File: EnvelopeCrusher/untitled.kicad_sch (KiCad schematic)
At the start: 7 parts

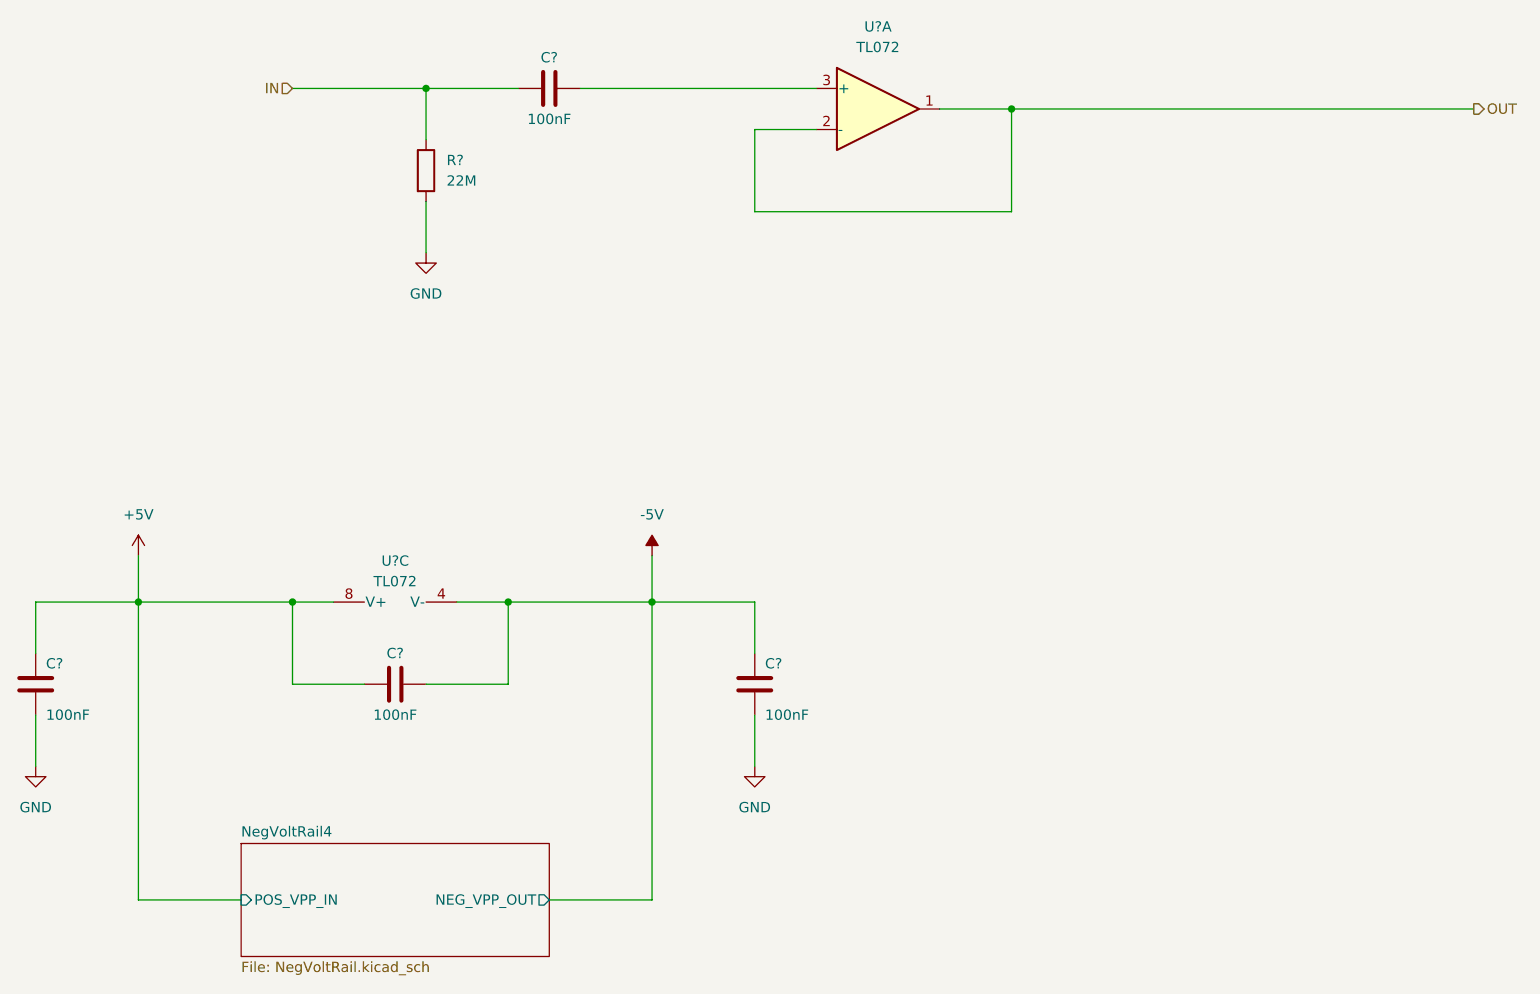
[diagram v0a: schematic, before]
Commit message: updated signal path
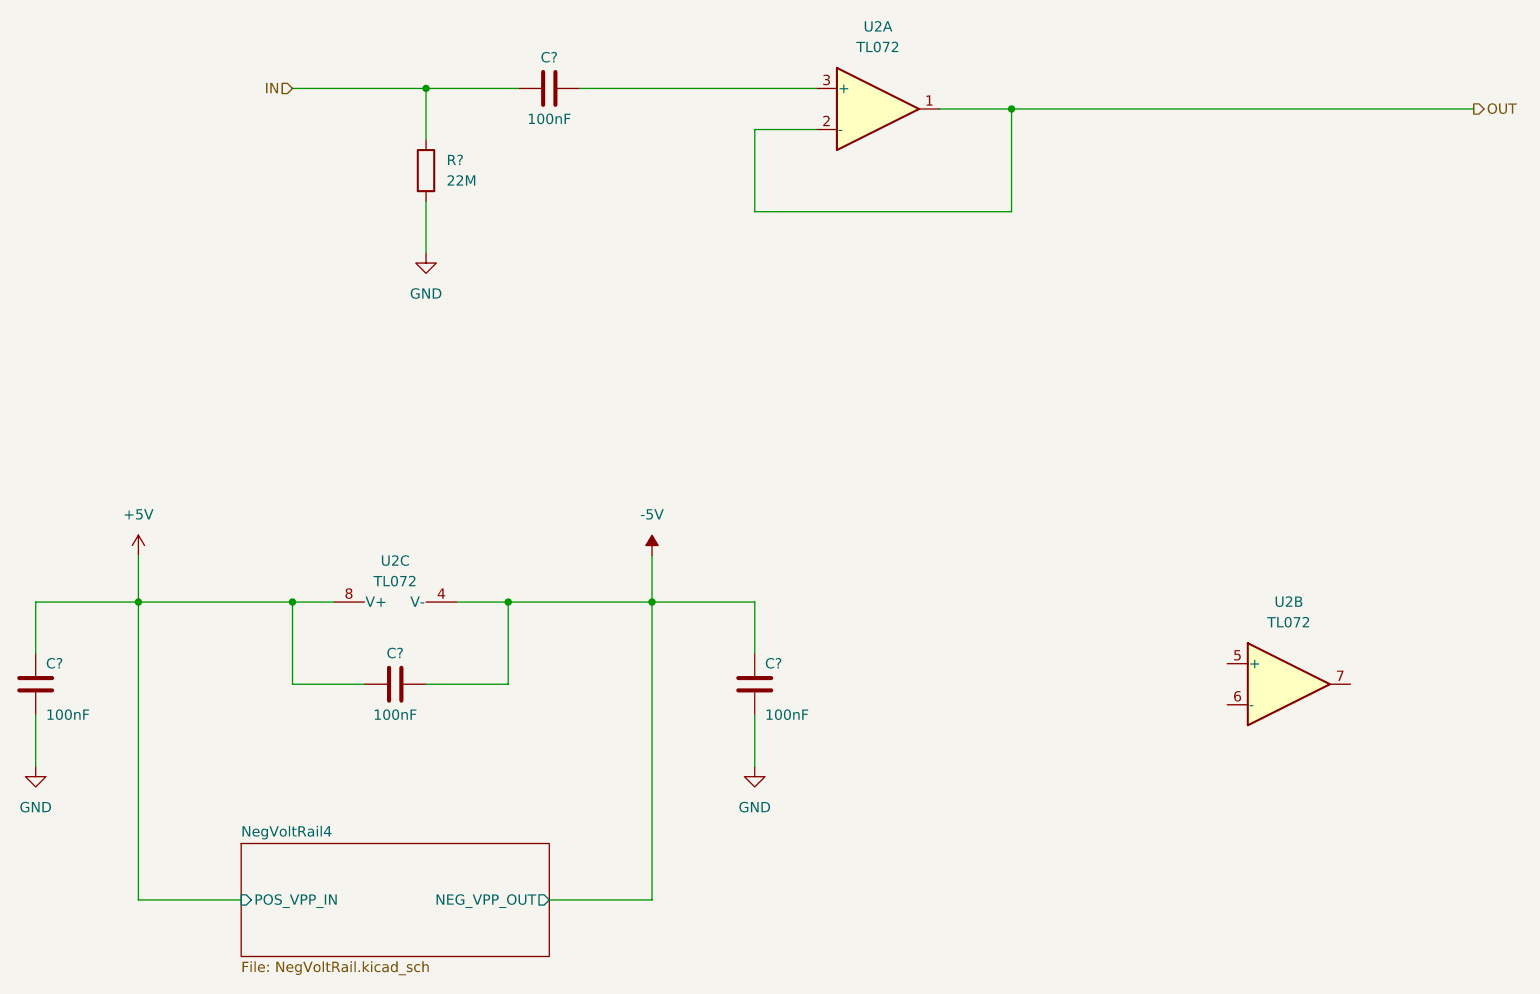
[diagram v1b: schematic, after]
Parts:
- added unit 2 of U2
- gave numbers to parts that had none: 1
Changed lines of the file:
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@@
   (symbol (lib_id "Amplifier_Operational:TL072") (at 109.22 123.19 90) (unit 3)
     (in_bom yes) (on_board yes) (fields_autoplaced)
-    (property "Reference" "U?" (id 0) (at 109.22 120.65 90))
+    (property "Reference" "U2" (id 0) (at 109.22 120.65 90))
     (property "Value" "TL072" (id 1) (at 109.22 123.19 90))
     (property "Footprint" "" (id 2) (at 109.22 123.19 0)
@@
     (pin "1")
   )
+  (symbol (lib_id "Amplifier_Operational:TL072") (at 219.71 135.89 0) (unit 2)
+    (in_bom yes) (on_board yes) (fields_autoplaced)
+    (property "Reference" "U2" (id 0) (at 219.71 125.73 0))
+    (property "Value" "TL072" (id 1) (at 219.71 128.27 0))
+    (property "Footprint" "" (id 2) (at 219.71 135.89 0)
+      (effects (font (size 1.27 1.27)) hide)
+    )
+    (property "Datasheet" "http://www.ti.com/lit/ds/symlink/tl071.pdf" (id 3) (at 219.71 135.89 0)
+      (effects (font (size 1.27 1.27)) hide)
+    )
+    (pin "1")
+    (pin "2")
+    (pin "3")
+    (pin "5")
+    (pin "6")
+    (pin "7")
+    (pin "4")
+    (pin "8")
+  )
   (symbol (lib_id "Device:C") (at 64.77 135.89 180) (unit 1)
     (in_bom yes) (on_board yes)
@@
   (symbol (lib_id "Amplifier_Operational:TL072") (at 168.91 64.77 0) (unit 1)
     (in_bom yes) (on_board yes) (fields_autoplaced)
-    (property "Reference" "U?" (id 0) (at 168.91 54.61 0))
+    (property "Reference" "U2" (id 0) (at 168.91 54.61 0))
     (property "Value" "TL072" (id 1) (at 168.91 57.15 0))
     (property "Footprint" "" (id 2) (at 168.91 64.77 0)
